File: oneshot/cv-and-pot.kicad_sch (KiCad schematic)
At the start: 10 parts, among them U6 LM358

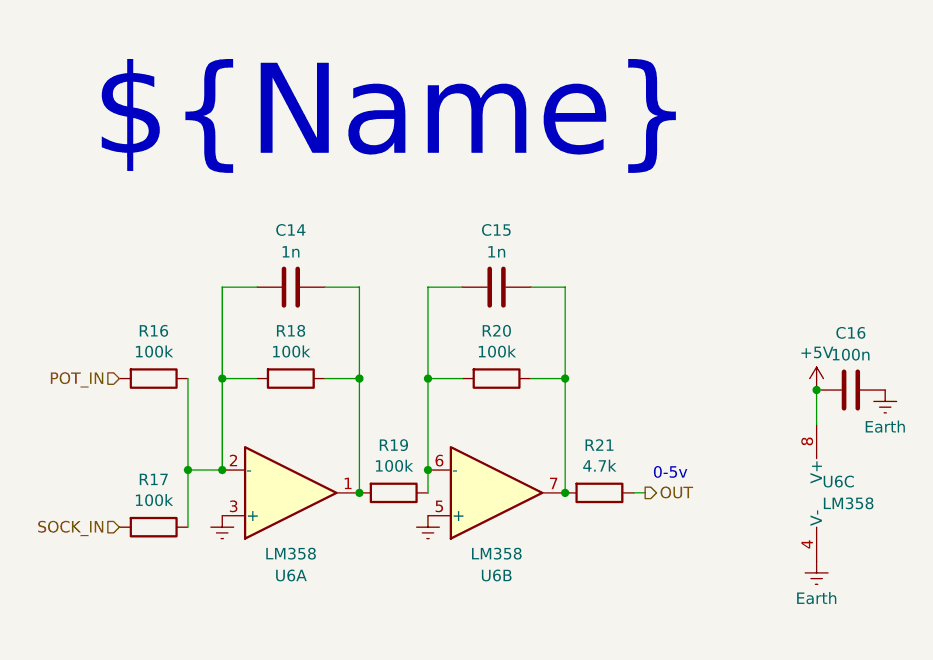
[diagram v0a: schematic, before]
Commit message: Updating oneshot project files
These are for the 1.1 (Prototype 2) PCBs
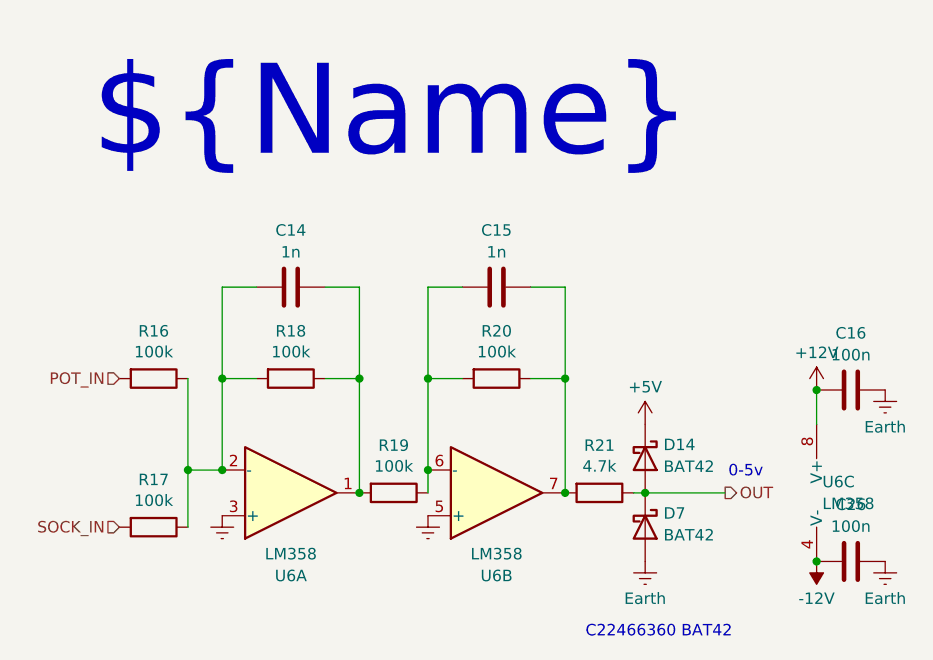
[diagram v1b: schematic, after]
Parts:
- added C26: 100n, Capacitor_SMD:C_0402_1005Metric, symbol Device:C
- added D14, D7: BAT42, Diode_SMD:D_SOD-323, symbol Diode:BAT42
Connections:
- net +5V: now also D14.1 (K); no longer C16.1, U6.8 (V+)
- net Earth: now also C26.2, D7.2 (A); no longer U6.4 (V-)
- net OUT: now also D14.2 (A), D7.1 (K)
- new net +12V: C16.1, U6.8 (V+)
- new net -12V: C26.1, U6.4 (V-)
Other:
- note added: "C22466360 BAT42"
